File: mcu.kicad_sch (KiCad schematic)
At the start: 40 parts, among them J301 USB_C_Receptacle_USB2.0_16P, J302 2x5x1.27mm, U301 STM32F103CBTx, U302 USBLC6-2SC6, Y301 16MHz

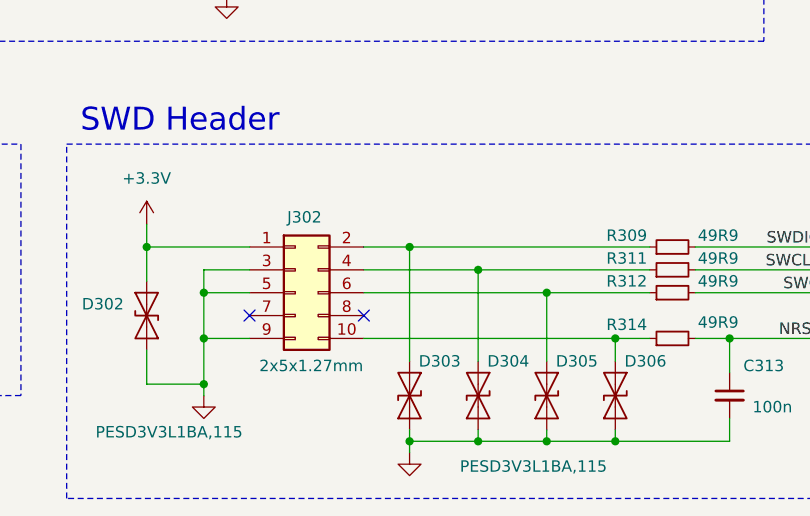
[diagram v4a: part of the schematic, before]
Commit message: Lesson 12: MCU and USB rough placement
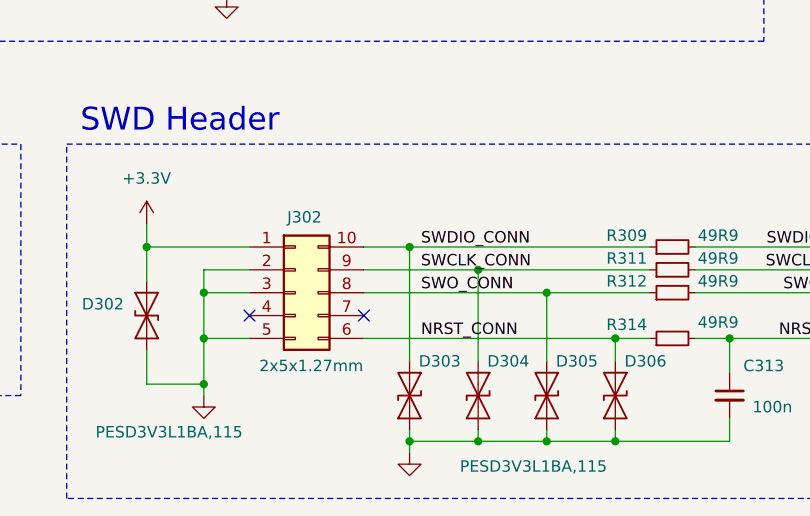
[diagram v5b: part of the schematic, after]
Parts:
- J301: footprint Connector_USB:USB_C_Receptacle_G-Switch_GT-USB-7010ASV -> Connector_USB:USB_C_Receptacle_HRO_TYPE-C-31-M-12
- J302: symbol Connector_Generic:Conn_02x05_Odd_Even -> Connector_Generic:Conn_02x05_Counter_Clockwise
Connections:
- net GND: now also J302.2 (Pin_2); no longer J302.9 (Pin_9)
- net SWDIO_CONN: now reaches D303.2 (A2), R309.1
- net SWDIO_CONN: now also J302.10 (Pin_10); no longer J302.2 (Pin_2)
- net SWO_CONN: now reaches D305.2 (A2), R312.1
- net SWO_CONN: now also J302.8 (Pin_8); no longer J302.6 (Pin_6)
- net SWCLK_CONN: now reaches D304.2 (A2), R311.1
- net SWCLK_CONN: now also J302.9 (Pin_9); no longer J302.4 (Pin_4)
- net NRST_CONN: now reaches D306.2 (A2), R314.1
- net NRST_CONN: now also J302.6 (Pin_6); no longer J302.10 (Pin_10)
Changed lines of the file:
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@@
 		)
 	)
+	(label "SWO_CONN"
+		(at 120.65 166.37 0)
+		(fields_autoplaced yes)
+		(effects
+			(font
+				(size 1.27 1.27)
+			)
+			(justify left bottom)
+		)
+	)
 	(label "USB_D+"
 		(at 243.84 123.19 180)
@@
 		)
 	)
+	(label "SWCLK_CONN"
+		(at 120.65 163.83 0)
+		(fields_autoplaced yes)
+		(effects
+			(font
+				(size 1.27 1.27)
+			)
+			(justify left bottom)
+		)
+	)
 	(label "USB_CMC_D-"
 		(at 186.69 118.11 0)
@@
 		)
 	)
+	(label "SWDIO_CONN"
+		(at 120.65 161.29 0)
+		(fields_autoplaced yes)
+		(effects
+			(font
+				(size 1.27 1.27)
+			)
+			(justify left bottom)
+		)
+	)
 	(label "USB_D-"
 		(at 132.08 86.36 180)
@@
 		)
 	)
+	(label "NRST_CONN"
+		(at 120.65 171.45 0)
+		(fields_autoplaced yes)
+		(effects
+			(font
+				(size 1.27 1.27)
+			)
+			(justify left bottom)
+		)
+	)
 	(label "TIM4_CH1"
 		(at 26.67 158.75 0)
@@
 			)
 		)
-		(property "Footprint" "Connector_USB:USB_C_Receptacle_G-Switch_GT-USB-7010ASV"
+		(property "Footprint" "Connector_USB:USB_C_Receptacle_HRO_TYPE-C-31-M-12"
 			(at 236.22 67.31 0)
 			(effects
@@
 	)
 	(symbol
-		(lib_id "Connector_Generic:Conn_02x05_Odd_Even")
+		(lib_id "Connector_Generic:Conn_02x05_Counter_Clockwise")
 		(at 106.68 166.37 0)
 		(unit 1)
@@
 			)
 		)
-		(property "Description" "Generic connector, double row, 02x05, odd/even pin numbering scheme (row 1 odd numbers, row 2 even numbers), script generated (kicad-library-utils/schlib/autogen/connector/)"
+		(property "Description" "Generic connector, double row, 02x05, counter clockwise pin numbering scheme (similar to DIP package numbering), script generated (kicad-library-utils/schlib/autogen/connector/)"
 			(at 106.68 166.37 0)
 			(effects

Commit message: Lesson 13: Routing
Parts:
- J302: symbol Connector_Generic:Conn_02x05_Counter_Clockwise -> Connector_Generic:Conn_02x05_Odd_Even
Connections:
- net DAC_NCLR: now also U301.20 (PB2); no longer U301.21 (PB10)
- net DAC_NLDAC: now also U301.21 (PB10); no longer U301.22 (PB11)
- net GND: now also J302.9 (Pin_9); no longer J302.2 (Pin_2)
- net NRST_CONN: now also J302.10 (Pin_10); no longer J302.6 (Pin_6)
- net SWCLK_CONN: now also J302.4 (Pin_4); no longer J302.9 (Pin_9)
- net SWDIO_CONN: now also J302.2 (Pin_2); no longer J302.10 (Pin_10)
- net SWO_CONN: now also J302.6 (Pin_6); no longer J302.8 (Pin_8)
- net TIM4_CH1: now also R310.1; no longer R308.1
- net TIM4_CH2: now also R313.1; no longer R310.1
- net TIM4_CH3: now also R308.1; no longer R313.1
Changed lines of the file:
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@@
 	)
 	(no_connect
+		(at 83.82 114.3)
+	)
+	(no_connect
 		(at 116.84 78.74)
 	)
@@
 	)
 	(no_connect
-		(at 83.82 91.44)
-	)
-	(no_connect
 		(at 116.84 76.2)
 	)
@@
 	(wire
 		(pts
-			(xy 71.12 93.98) (xy 83.82 93.98)
+			(xy 62.23 93.98) (xy 83.82 93.98)
 		)
 		(stroke
@@
 	(wire
 		(pts
-			(xy 41.91 71.12) (xy 41.91 86.36)
+			(xy 80.01 91.44) (xy 83.82 91.44)
 		)
 		(stroke
@@
 	(wire
 		(pts
-			(xy 132.08 50.8) (xy 132.08 52.07)
+			(xy 41.91 71.12) (xy 41.91 86.36)
 		)
 		(stroke
@@
 	(wire
 		(pts
-			(xy 62.23 50.8) (xy 62.23 52.07)
+			(xy 132.08 50.8) (xy 132.08 52.07)
 		)
 		(stroke
@@
 	(wire
 		(pts
-			(xy 81.28 114.3) (xy 83.82 114.3)
+			(xy 62.23 50.8) (xy 62.23 52.07)
 		)
 		(stroke
@@
 		)
 	)
+	(label "TIM4_CH1"
+		(at 26.67 163.83 0)
+		(fields_autoplaced yes)
+		(effects
+			(font
+				(size 1.27 1.27)
+			)
+			(justify left bottom)
+		)
+	)
 	(label "USB_D-"
 		(at 132.08 86.36 180)
@@
 	)
 	(label "SWO"
-		(at 71.12 93.98 0)
+		(at 62.23 93.98 0)
 		(fields_autoplaced yes)
 		(effects
@@
 		)
 	)
-	(label "USB_CONN_D-"
-		(at 209.55 64.77 0)
-		(fields_autoplaced yes)
-		(effects
-			(font
-				(size 1.27 1.27)
-			)
-			(justify left bottom)
-		)
-	)
-	(label "NRST_CONN"
-		(at 120.65 171.45 0)
+	(label "TIM4_CH3"
+		(at 26.67 158.75 0)
 		(fields_autoplaced yes)
 		(effects
@@
 		)
 	)
-	(label "TIM4_CH1"
-		(at 26.67 158.75 0)
+	(label "USB_CONN_D-"
+		(at 209.55 64.77 0)
 		(fields_autoplaced yes)
 		(effects
@@
 		)
 	)
-	(label "TIM4_CH3"
-		(at 26.67 168.91 0)
+	(label "NRST_CONN"
+		(at 120.65 171.45 0)
 		(fields_autoplaced yes)
 		(effects
@@
 	)
 	(label "TIM4_CH2"
-		(at 26.67 163.83 0)
+		(at 26.67 168.91 0)
 		(fields_autoplaced yes)
 		(effects
@@
 	)
 	(global_label "DAC_NLDAC"
-		(shape input)
-		(at 81.28 114.3 180)
+		(shape output)
+		(at 81.28 111.76 180)
 		(fields_autoplaced yes)
 		(effects
@@
 		)
 		(property "Intersheetrefs" "${INTERSHEET_REFS}"
-			(at 67.7114 114.3 0)
+			(at 67.7114 111.76 0)
 			(effects
 				(font
@@
 	)
 	(global_label "DAC_NCLR"
-		(shape input)
-		(at 81.28 111.76 180)
+		(shape output)
+		(at 80.01 91.44 180)
 		(fields_autoplaced yes)
 		(effects
@@
 		)
 		(property "Intersheetrefs" "${INTERSHEET_REFS}"
-			(at 68.8 111.76 0)
+			(at 67.53 91.44 0)
 			(effects
 				(font
@@
 	)
 	(global_label "SPI2_MOSI"
-		(shape input)
+		(shape output)
 		(at 58.42 124.46 180)
 		(fields_autoplaced yes)
@@
 	)
 	(symbol
-		(lib_id "Connector_Generic:Conn_02x05_Counter_Clockwise")
+		(lib_id "Connector_Generic:Conn_02x05_Odd_Even")
 		(at 106.68 166.37 0)
 		(unit 1)
@@
 			)
 		)
-		(property "Description" "Generic connector, double row, 02x05, counter clockwise pin numbering scheme (similar to DIP package numbering), script generated (kicad-library-utils/schlib/autogen/connector/)"
+		(property "Description" "Generic connector, double row, 02x05, odd/even pin numbering scheme (row 1 odd numbers, row 2 even numbers), script generated (kicad-library-utils/schlib/autogen/connector/)"
 			(at 106.68 166.37 0)
 			(effects

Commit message: Assembly files
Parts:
- C301: MPN (none) -> C19702
- C302, C303, C304, C305, C311, C312, C313: MPN (none) -> C1525
- C306: value 10n -> 10nF; MPN (none) -> C15195
- C307, C308: MPN (none) -> C15849
- C309, C310: MPN (none) -> C32949
- D301: MPN (none) -> C375571
- J301: MPN (none) -> C319148
- J302: MPN (none) -> C920813
- L301: MPN (none) -> C404632
- R301, R302, R307: MPN (none) -> C25744
- R303, R304: MPN (none) -> C25905
- R305: MPN (none) -> C17168
- R306: MPN (none) -> C25867
- R308, R310, R313: MPN (none) -> C11702
- R309, R311, R312, R314: MPN (none) -> C25120
- U301: value STM32F103CBTx -> STM32F103CBT6; MPN (none) -> C8304
- U302: MPN (none) -> USBLC6-2SC6
- Y301: MPN (none) -> C362342
